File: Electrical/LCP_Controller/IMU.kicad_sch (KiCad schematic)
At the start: 9 parts, among them J9 Conn_01x04, Q8 TSM500P02CX RFG

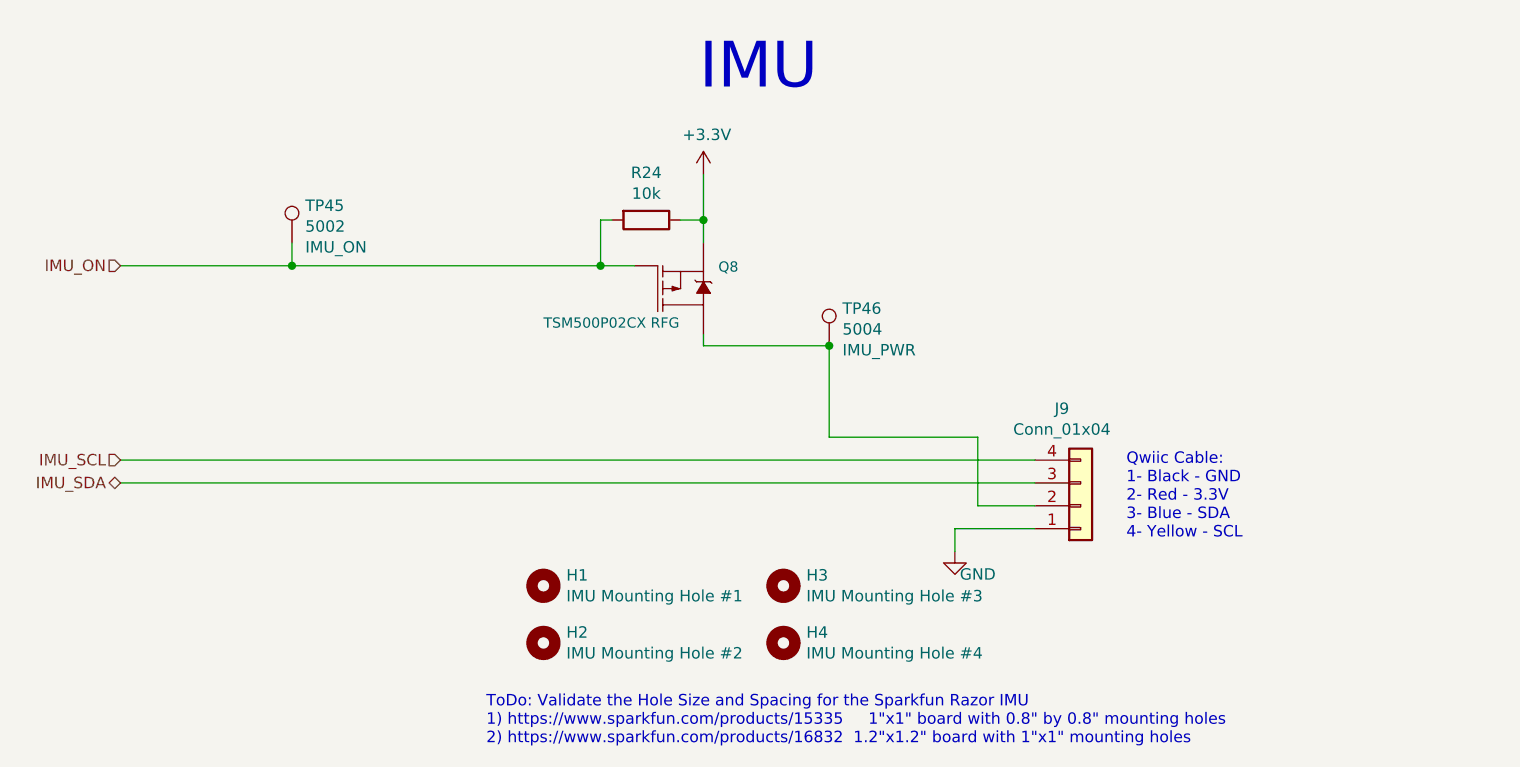
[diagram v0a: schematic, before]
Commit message: Hardware Revision : v0.3
1. modified schematic design, removed unnecessary test points.
2. pcb layout 2x8 Inches allowance dimension, layout is in progress
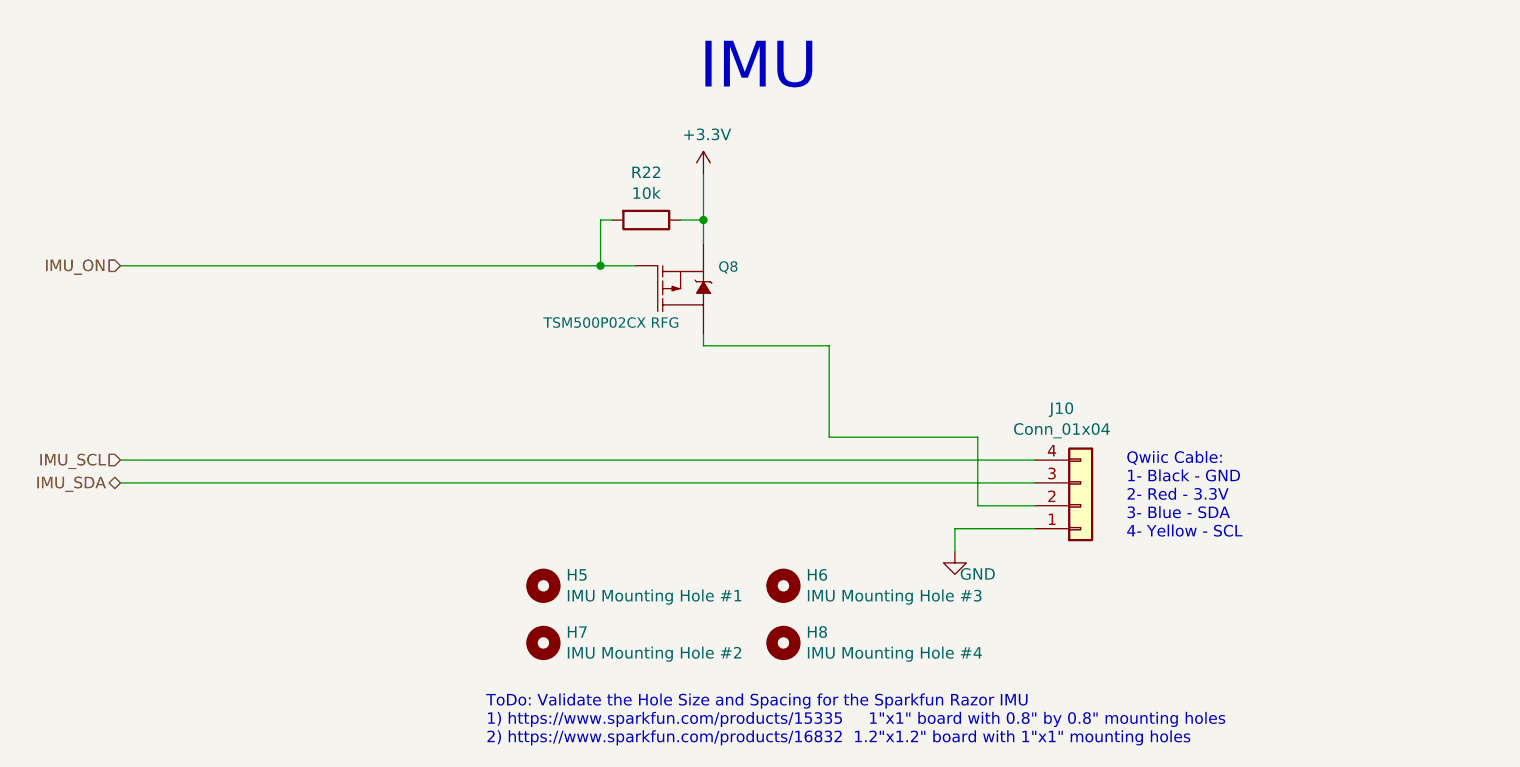
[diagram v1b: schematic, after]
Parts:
- removed TP45: 5002, TestPoint:TestPoint_Keystone_5000-5004_Miniature, symbol Connector:TestPoint
- removed TP46: 5004, TestPoint:TestPoint_Keystone_5000-5004_Miniature, symbol Connector:TestPoint
- renumbered H1 to H5, H3 to H6, H2 to H7, H4 to H8, J9 to J10, R24 to R22
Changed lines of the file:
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@@
     (comment 5 "Current design modified by: Basharat Martin")
   )
-  (junction (at 154.94 88.9) (diameter 0) (color 0 0 0 0)
-  )
   (junction (at 129.54 80.01) (diameter 0) (color 0 0 0 0)
   )
-  (junction (at 95.25 80.01) (diameter 0) (color 0 0 0 0)
-  )
   (junction (at 140.97 74.93) (diameter 0) (color 0 0 0 0)
   )
@@
     (stroke (width 0) (type default) (color 0 0 0 0))
   )
-  (wire (pts (xy 76.2 80.01) (xy 95.25 80.01))
-    (stroke (width 0) (type default) (color 0 0 0 0))
-  )
   (wire (pts (xy 138.43 74.93) (xy 140.97 74.93))
     (stroke (width 0) (type default) (color 0 0 0 0))
@@
     (stroke (width 0) (type default) (color 0 0 0 0))
   )
-  (wire (pts (xy 95.25 77.47) (xy 95.25 80.01))
-    (stroke (width 0) (type default) (color 0 0 0 0))
-  )
   (wire (pts (xy 154.94 88.9) (xy 154.94 99.06))
     (stroke (width 0) (type default) (color 0 0 0 0))
@@
     (stroke (width 0) (type default) (color 0 0 0 0))
   )
-  (wire (pts (xy 95.25 80.01) (xy 129.54 80.01))
+  (wire (pts (xy 76.2 80.01) (xy 129.54 80.01))
     (stroke (width 0) (type default) (color 0 0 0 0))
   )
@@
     (effects (font (size 1.27 1.27)) (justify right))
   )
-  (symbol (lib_id "Connector:TestPoint") (at 154.94 88.9 0) (unit 1)
-    (in_bom yes) (on_board yes)
-    (property "Reference" "TP46" (id 0) (at 156.4132 84.7598 0)
-      (effects (font (size 1.27 1.27)) (justify left))
-    )
-    (property "Value" "5004" (id 1) (at 156.4132 87.0712 0)
-      (effects (font (size 1.27 1.27)) (justify left))
-    )
-    (property "Footprint" "TestPoint:TestPoint_Keystone_5000-5004_Miniature" (id 2) (at 160.02 88.9 0)
-      (effects (font (size 1.27 1.27)) hide)
-    )
-    (property "Datasheet" "~" (id 3) (at 160.02 88.9 0)
-      (effects (font (size 1.27 1.27)) hide)
-    )
-    (property "TestPoint" "IMU_PWR" (id 4) (at 156.4132 89.3826 0)
-      (effects (font (size 1.27 1.27)) (justify left))
-    )
-    (property "MPN" "" (id 5) (at 154.94 88.9 0)
-      (effects (font (size 1.27 1.27)) hide)
-    )
-    (pin "1")
-  )
   (symbol (lib_id "Mechanical:MountingHole") (at 123.19 115.57 0) (unit 1)
     (in_bom yes) (on_board yes)
-    (property "Reference" "H1" (id 0) (at 125.73 114.4016 0)
+    (property "Reference" "H5" (id 0) (at 125.73 114.4016 0)
       (effects (font (size 1.27 1.27)) (justify left))
     )
@@
   (symbol (lib_id "Mechanical:MountingHole") (at 123.19 121.92 0) (unit 1)
     (in_bom yes) (on_board yes)
-    (property "Reference" "H2" (id 0) (at 125.73 120.7516 0)
+    (property "Reference" "H7" (id 0) (at 125.73 120.7516 0)
       (effects (font (size 1.27 1.27)) (justify left))
     )
@@
   (symbol (lib_id "Mechanical:MountingHole") (at 149.86 115.57 0) (unit 1)
     (in_bom yes) (on_board yes)
-    (property "Reference" "H3" (id 0) (at 152.4 114.4016 0)
+    (property "Reference" "H6" (id 0) (at 152.4 114.4016 0)
       (effects (font (size 1.27 1.27)) (justify left))
     )
@@
   (symbol (lib_id "Mechanical:MountingHole") (at 149.86 121.92 0) (unit 1)
     (in_bom yes) (on_board yes)
-    (property "Reference" "H4" (id 0) (at 152.4 120.7516 0)
+    (property "Reference" "H8" (id 0) (at 152.4 120.7516 0)
       (effects (font (size 1.27 1.27)) (justify left))
     )
@@
   (symbol (lib_id "Connector_Generic:Conn_01x04") (at 182.88 106.68 0) (mirror x) (unit 1)
     (in_bom yes) (on_board yes)
-    (property "Reference" "J9" (id 0) (at 180.7972 95.885 0))
+    (property "Reference" "J10" (id 0) (at 180.7972 95.885 0))
     (property "Value" "Conn_01x04" (id 1) (at 180.7972 98.1964 0))
     (property "Footprint" "Connector_JST:JST_SH_BM04B-SRSS-TB_1x04-1MP_P1.00mm_Vertical" (id 2) (at 182.88 106.68 0)
@@
   (symbol (lib_id "power:GND") (at 168.91 111.76 0) (unit 1)
     (in_bom yes) (on_board yes)
-    (property "Reference" "#PWR065" (id 0) (at 168.91 118.11 0)
+    (property "Reference" "#PWR070" (id 0) (at 168.91 118.11 0)
       (effects (font (size 1.27 1.27)) hide)
     )
@@
   (symbol (lib_id "power:+3.3V") (at 140.97 69.85 0) (unit 1)
     (in_bom yes) (on_board yes)
-    (property "Reference" "#PWR063" (id 0) (at 140.97 73.66 0)
+    (property "Reference" "#PWR069" (id 0) (at 140.97 73.66 0)
       (effects (font (size 1.27 1.27)) hide)
     )
@@
   (symbol (lib_id "Device:R") (at 134.62 74.93 270) (unit 1)
     (in_bom yes) (on_board yes)
-    (property "Reference" "R24" (id 0) (at 134.62 69.6722 90))
+    (property "Reference" "R22" (id 0) (at 134.62 69.6722 90))
     (property "Value" "10k" (id 1) (at 134.62 71.9836 90))
     (property "Footprint" "Resistor_SMD:R_0805_2012Metric" (id 2) (at 134.62 73.152 90)
@@
     (pin "2")
   )
-  (symbol (lib_id "Connector:TestPoint") (at 95.25 77.47 0) (unit 1)
-    (in_bom yes) (on_board yes)
-    (property "Reference" "TP45" (id 0) (at 96.7232 73.3298 0)
-      (effects (font (size 1.27 1.27)) (justify left))
-    )
-    (property "Value" "5002" (id 1) (at 96.7232 75.6412 0)
-      (effects (font (size 1.27 1.27)) (justify left))
-    )
-    (property "Footprint" "TestPoint:TestPoint_Keystone_5000-5004_Miniature" (id 2) (at 100.33 77.47 0)
-      (effects (font (size 1.27 1.27)) hide)
-    )
-    (property "Datasheet" "~" (id 3) (at 100.33 77.47 0)
-      (effects (font (size 1.27 1.27)) hide)
-    )
-    (property "TestPoint" "IMU_ON" (id 4) (at 96.7232 77.9526 0)
-      (effects (font (size 1.27 1.27)) (justify left))
-    )
-    (property "MPN" "" (id 5) (at 95.25 77.47 0)
-      (effects (font (size 1.27 1.27)) hide)
-    )
-    (pin "1")
-  )
 )

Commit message: Hw Rev : 0.3v updated
changed TRS3122ERGER to TRS3122ERGET due to shortage of part.
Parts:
- H5, H6, H7: Population (none) -> DNP
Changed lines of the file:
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@@
+      (effects (font (size 1.27 1.27)) hide)
+    )
+    (property "Population" "DNP" (id 5) (at 123.19 115.57 0)
       (effects (font (size 1.27 1.27)) hide)
     )
@@
       (effects (font (size 1.27 1.27)) hide)
     )
+    (property "Population" "DNP" (id 5) (at 123.19 121.92 0)
+      (effects (font (size 1.27 1.27)) hide)
+    )
   )
   (symbol (lib_id "Mechanical:MountingHole") (at 149.86 115.57 0) (unit 1)
@@
       (effects (font (size 1.27 1.27)) hide)
     )
+    (property "Population" "DNP" (id 5) (at 149.86 115.57 0)
+      (effects (font (size 1.27 1.27)) hide)
+    )
